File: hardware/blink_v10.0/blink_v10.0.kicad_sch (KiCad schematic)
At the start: 135 parts, among them J1 Conn_01x02, J14 Conn_02x16_Odd_Even, J15 Conn_01x01, J16 Conn_01x01, J5 Conn_01x06_Pin, J6 Conn_01x03, J7 Conn_01x06_Pin, J9 USB_C_Receptacle, Q1 S8550, Q2 S8050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

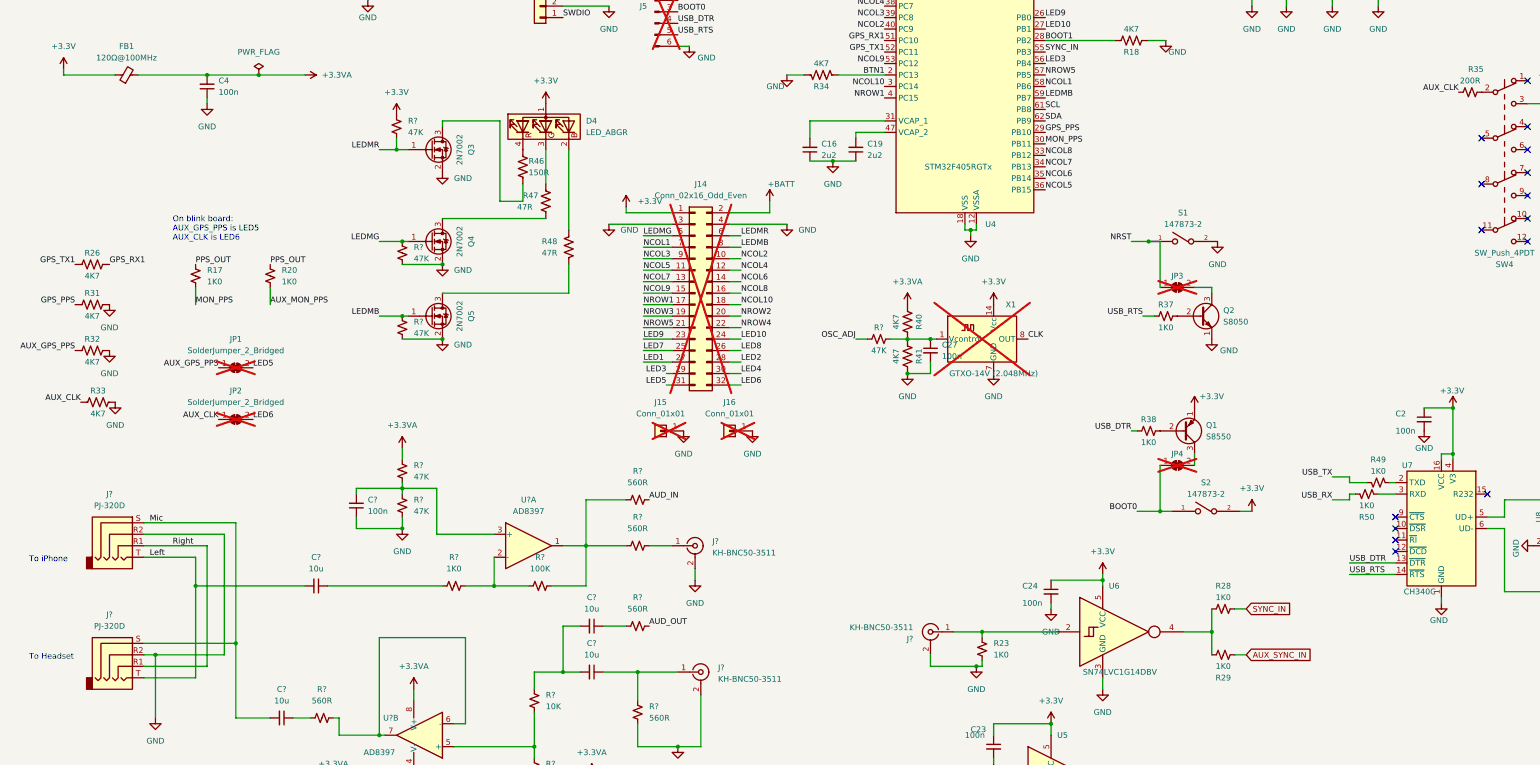
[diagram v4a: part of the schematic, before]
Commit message: clean up LED5/6 problem and BTN2
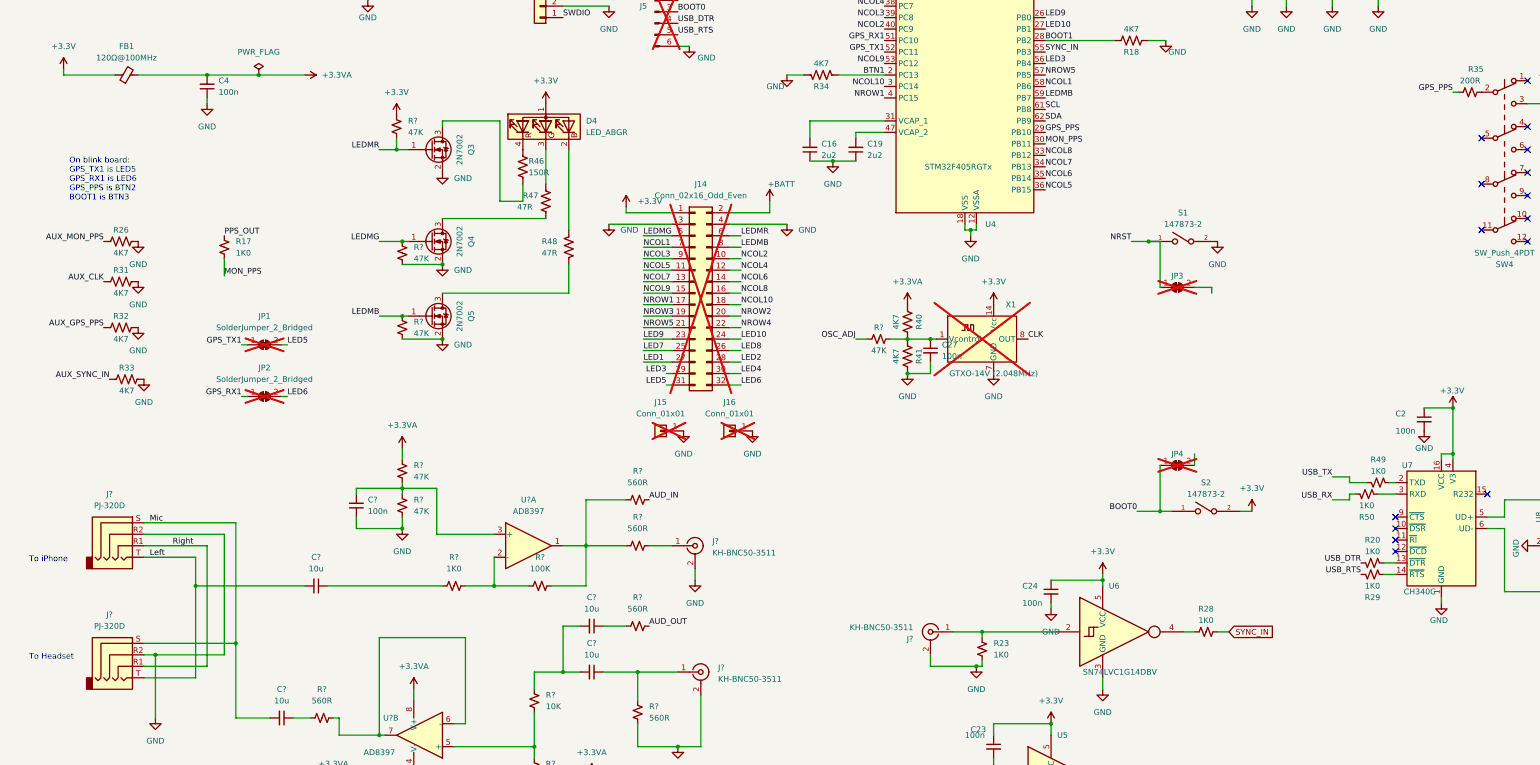
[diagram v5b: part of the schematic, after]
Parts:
- removed Q1: S8550, Package_TO_SOT_SMD:SOT-23-3, symbol Transistor_BJT:S8550
- removed Q2: S8050, Package_TO_SOT_SMD:SOT-23-3, symbol Transistor_BJT:S8050
- removed R37, R38: 1K0, Resistor_SMD:R_0603_1608Metric, symbol Device:R_Small_US
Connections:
- net AUX_CLK: now also R31.1; no longer JP2.1 (A), R33.1, R35.2
- net AUX_GPS_PPS: no longer JP1.1 (A)
- net AUX_MON_PPS: now also R26.1; no longer R20.2
- net AUX_SYNC_IN: now also R33.1; no longer R29.1
- net GND: now also R26.2
- net GPS_PPS: now also R35.2; no longer R31.1
- net GPS_RX1: now also JP2.1 (A); no longer R26.2
- net GPS_TX1: now also JP1.1 (A); no longer R26.1
- net PPS_OUT: no longer R20.1
- net USB_DTR: now also R20.2; no longer U7.13 (~{DTR})
- net USB_RTS: now also R29.1; no longer U7.14 (~{RTS})
- net at R28.2, U6.4: no longer R29.2
- new net: R20.1, U7.13 (~{DTR})
- new net: R29.2, U7.14 (~{RTS})
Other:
- note added: "On blink board: GPS_TX1 is LED5 GPS_RX1 is LED6 GPS_PPS is BTN2 BOOT1 is BTN3"
- note removed: "On blink board: AUX_GPS_PPS is LED5 AUX_CLK is LED6"
- moved on the sheet: JP1, JP2, R17, R26, R28, R31, R32, R33

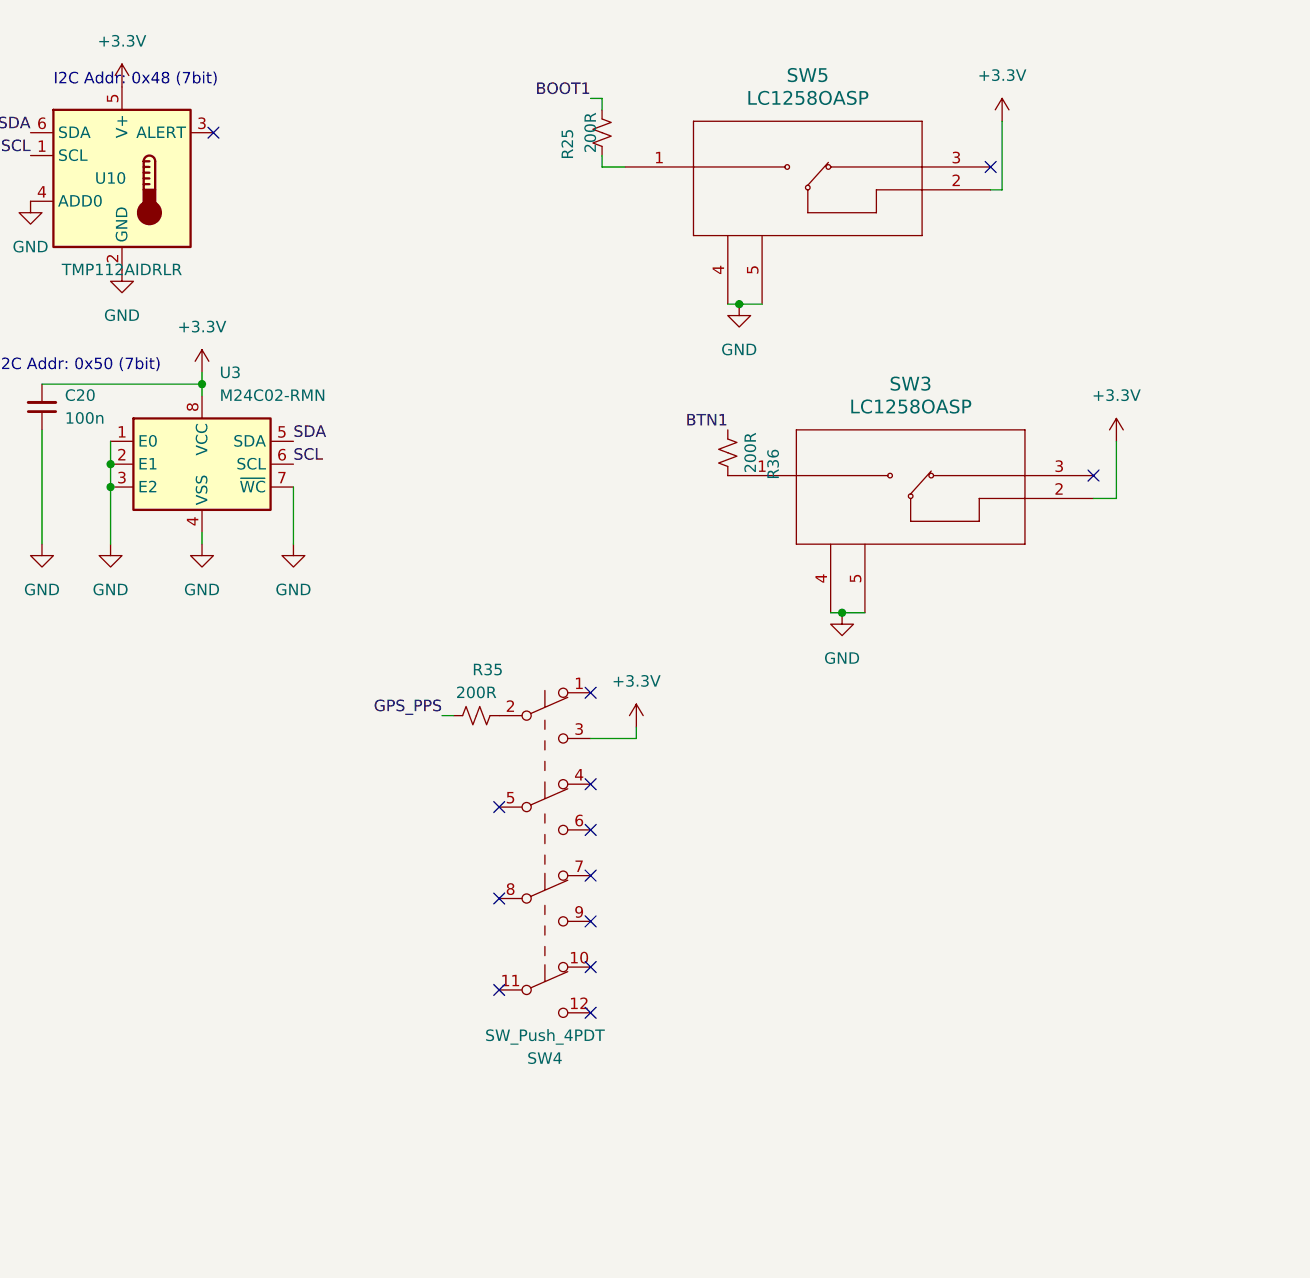
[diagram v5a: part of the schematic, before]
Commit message: fix buttons. Fixes #264 Fixes #261
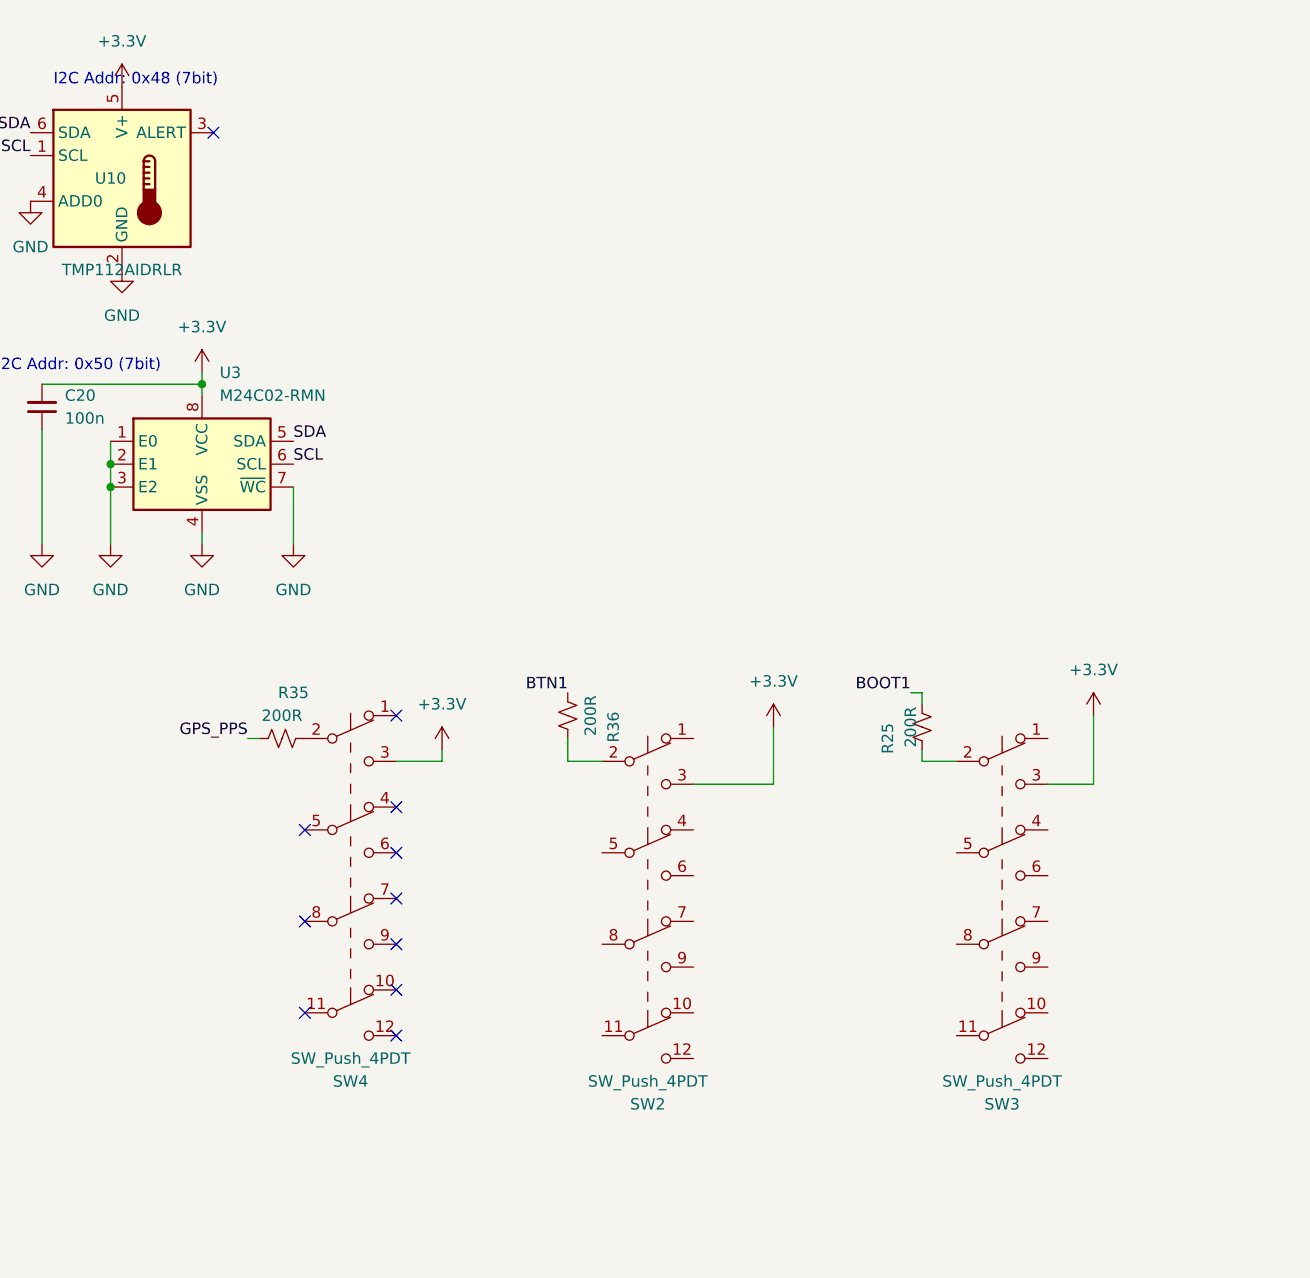
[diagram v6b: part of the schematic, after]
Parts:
- removed SW3, SW5: LC1258OASP, blinky_footprints:LC1258OASP, symbol BlinkyShared:LC1258OASP
- added SW2, SW3: SW_Push_4PDT, blinky_footprints:PBH4UOANAGX, symbol BlinkyShared:SW_Push_4PDT
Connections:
- net +3.3V: now also SW2.3 (C), SW3.3 (C)
- net at R36.1: now also SW2.2 (B)
- net at R25.1: now also SW3.2 (B)
- no-connect marks 22 -> 20
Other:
- moved on the sheet: R25, R35, R36, SW4

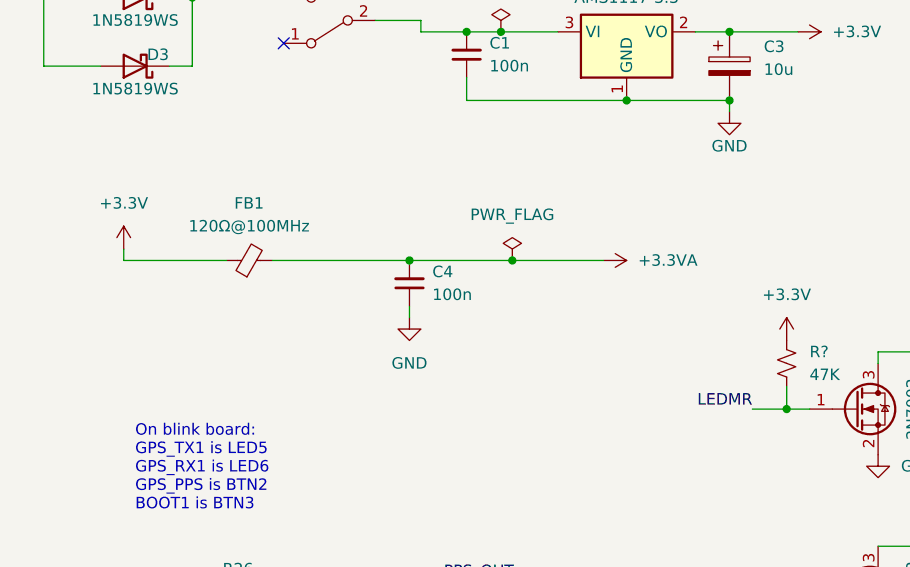
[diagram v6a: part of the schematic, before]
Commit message: add a sense resistor to blink v10
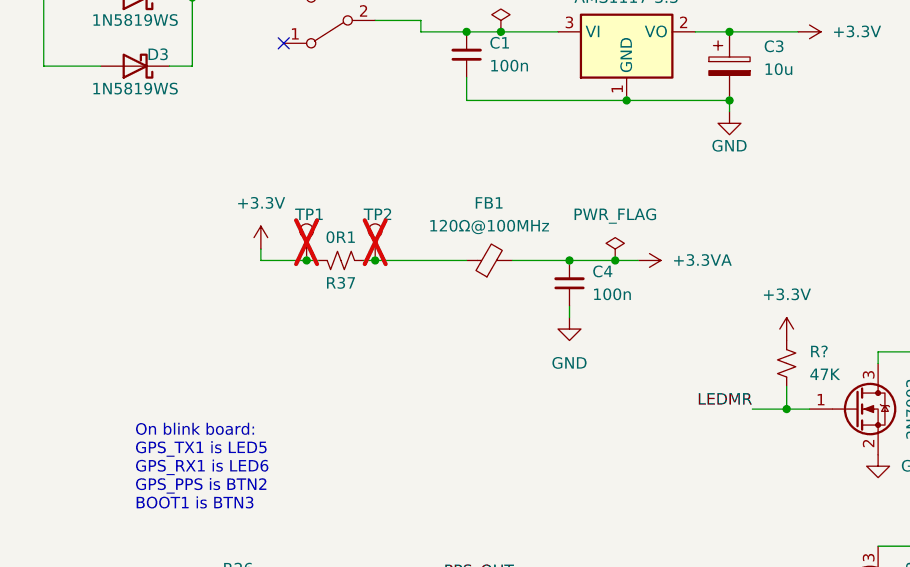
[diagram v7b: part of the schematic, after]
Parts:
- added R37: 0R1, Resistor_SMD:R_1206_3216Metric, symbol Device:R_Small_US
- added TP1, TP2: ~, TestPoint:TestPoint_THTPad_D1.0mm_Drill0.5mm, symbol Connector:TestPoint
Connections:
- net +3.3V: now also R37.2, TP1.1; no longer FB1.1
- new net: FB1.1, R37.1, TP2.1
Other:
- moved on the sheet: C4, FB1

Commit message: add sense resitors to other ps on bink
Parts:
- added R38: 0R1, Resistor_SMD:R_1206_3216Metric, symbol Device:R_Small_US
- added TP3, TP4: ~, TestPoint:TestPoint_THTPad_D1.0mm_Drill0.5mm, symbol Connector:TestPoint
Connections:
- net at C1.2, U1.3 (VI): now also R38.1, TP4.1; no longer SW1.2 (B)
- new net +4V: R38.2, SW1.2 (B), TP3.1
- no-connect marks 20 -> 40
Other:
- moved on the sheet: C1, C20, C27, C3, C30, C4, D2, D3, D4, FB1, JP3, Q3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
